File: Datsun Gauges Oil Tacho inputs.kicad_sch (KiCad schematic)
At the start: 11 parts, among them SW1 Oil Pressure Sw, U1 CNY74-4H, U2 CNY74-4H

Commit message: Updated kicad diagrams
Updated kicad diagrams
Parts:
- removed D1, D2: 1N4148, Diode_THT:D_DO-35_SOD27_P7.62mm_Horizontal, symbol Diode:1N4148
- removed R1, R2: 1k8, symbol Device:R
- removed R3, R4: 1k, symbol Device:R
- removed R6: 10R, symbol Device:R
- removed U1, U2: CNY74-4H, symbol Isolator:CNY17-4
- added C3: 100n, symbol Device:C_Small
- added D1, D2: 1N4734A 5.6v, Diode_THT:D_DO-41_SOD81_P10.16mm_Horizontal, symbol Diode:1N47xxA
- added D3: 1N4148, Diode_THT:D_DO-35_SOD27_P7.62mm_Horizontal, symbol Diode:1N4148
- added R1 (x2), R2 (x2): 2k, symbol Device:R
- added U1, U2: 4049, symbol 4xxx:4049
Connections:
- net Arduino Oil Pressure pin: now also U1.2
- net Arduino Tacho pin: now also U2.6
- net Earth: no longer C2.2
- net GND: now also C2.2, D1.2 (A), D2.2 (A), U2.8 (VSS)
- net Oil Pressure Sw input: now also D3.2 (A), R1.2, R2.2
- net Tacho input from ECU: now also R1.2, R2.2
- net VCC: now also U2.1 (VCC)
- net at C2.1: now also D1.1 (K), D3.1 (K), R2.1, U1.3
- new net: D2.1 (K), R2.1, U2.7
- new net VDD: R1.1, R1.1
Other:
- moved on the sheet: SW1

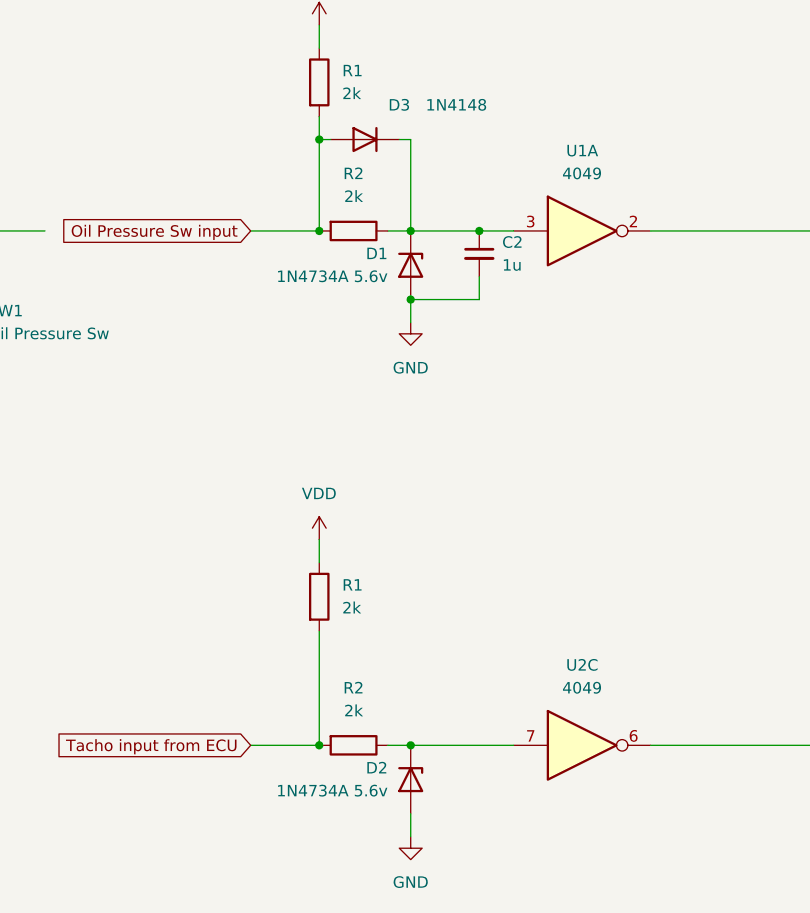
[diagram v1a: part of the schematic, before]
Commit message: Fixes
Changed some switch debouncing
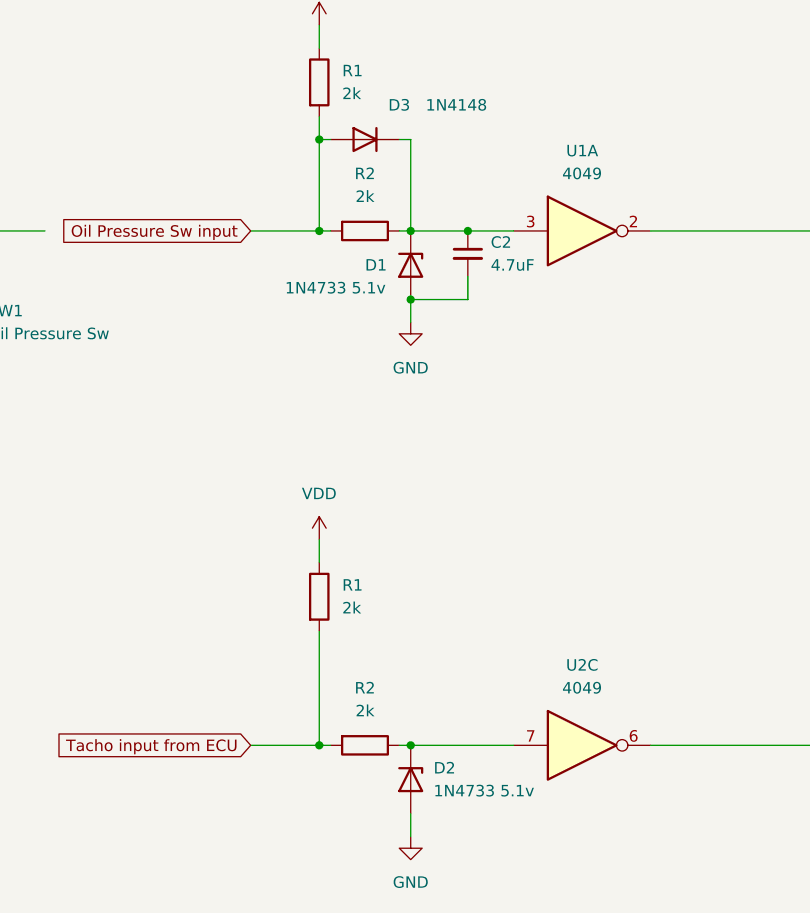
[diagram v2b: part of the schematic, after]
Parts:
- C2: value 1u -> 4.7uF
- D1, D2: value 1N4734A 5.6v -> 1N4733 5.1v
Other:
- moved on the sheet: C2, R2
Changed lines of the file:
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@@
   (junction (at 134.62 77.47) (diameter 0) (color 0 0 0 0)
   )
+  (junction (at 140.97 77.47) (diameter 0) (color 0 0 0 0)
+  )
   (junction (at 124.46 77.47) (diameter 0) (color 0 0 0 0)
   )
@@
   (junction (at 124.46 134.62) (diameter 0) (color 0 0 0 0)
   )
-  (junction (at 142.24 77.47) (diameter 0) (color 0 0 0 0)
-  )
   (junction (at 134.62 85.09) (diameter 0) (color 0 0 0 0)
   )
-  (wire (pts (xy 142.24 82.55) (xy 142.24 85.09))
-    (stroke (width 0) (type default))
-  )
-  (wire (pts (xy 134.62 77.47) (xy 142.24 77.47))
-    (stroke (width 0) (type default))
-  )
-  (wire (pts (xy 132.08 77.47) (xy 134.62 77.47))
+  (wire (pts (xy 140.97 82.55) (xy 140.97 85.09))
+    (stroke (width 0) (type default))
+  )
+  (wire (pts (xy 134.62 77.47) (xy 140.97 77.47))
+    (stroke (width 0) (type default))
+  )
+  (wire (pts (xy 133.35 77.47) (xy 134.62 77.47))
     (stroke (width 0) (type default))
   )
@@
     (stroke (width 0) (type default))
   )
-  (wire (pts (xy 134.62 134.62) (xy 132.08 134.62))
+  (wire (pts (xy 125.73 134.62) (xy 124.46 134.62))
+    (stroke (width 0) (type default))
+  )
+  (wire (pts (xy 134.62 134.62) (xy 133.35 134.62))
     (stroke (width 0) (type default))
   )
@@
     (stroke (width 0) (type default))
   )
-  (wire (pts (xy 142.24 77.47) (xy 146.05 77.47))
+  (wire (pts (xy 140.97 77.47) (xy 146.05 77.47))
     (stroke (width 0) (type default))
   )
@@
     (stroke (width 0) (type default))
   )
-  (wire (pts (xy 134.62 85.09) (xy 142.24 85.09))
+  (wire (pts (xy 134.62 85.09) (xy 140.97 85.09))
     (stroke (width 0) (type default))
   )
@@
   )
   (wire (pts (xy 86.36 77.47) (xy 93.98 77.47))
+    (stroke (width 0) (type default))
+  )
+  (wire (pts (xy 125.73 77.47) (xy 124.46 77.47))
     (stroke (width 0) (type default))
   )
@@
     )
   )
-  (symbol (lib_id "Device:R") (at 128.27 77.47 270) (unit 1)
-    (in_bom yes) (on_board yes) (dnp no) (fields_autoplaced)
-    (property "Reference" "R2" (at 128.27 71.12 90)
-      (effects (font (size 1.27 1.27)))
-    )
-    (property "Value" "2k" (at 128.27 73.66 90)
-      (effects (font (size 1.27 1.27)))
-    )
-    (property "Footprint" "" (at 128.27 75.692 90)
-      (effects (font (size 1.27 1.27)) hide)
-    )
-    (property "Datasheet" "~" (at 128.27 77.47 0)
+  (symbol (lib_id "Device:R") (at 129.54 77.47 270) (unit 1)
+    (in_bom yes) (on_board yes) (dnp no) (fields_autoplaced)
+    (property "Reference" "R2" (at 129.54 71.12 90)
+      (effects (font (size 1.27 1.27)))
+    )
+    (property "Value" "2k" (at 129.54 73.66 90)
+      (effects (font (size 1.27 1.27)))
+    )
+    (property "Footprint" "" (at 129.54 75.692 90)
+      (effects (font (size 1.27 1.27)) hide)
+    )
+    (property "Datasheet" "~" (at 129.54 77.47 0)
       (effects (font (size 1.27 1.27)) hide)
     )
@@
     )
   )
-  (symbol (lib_id "Device:C_Small") (at 142.24 80.01 0) (unit 1)
-    (in_bom yes) (on_board yes) (dnp no) (fields_autoplaced)
-    (property "Reference" "C2" (at 144.78 78.7463 0)
-      (effects (font (size 1.27 1.27)) (justify left))
-    )
-    (property "Value" "1u" (at 144.78 81.2863 0)
-      (effects (font (size 1.27 1.27)) (justify left))
-    )
-    (property "Footprint" "" (at 142.24 80.01 0)
-      (effects (font (size 1.27 1.27)) hide)
-    )
-    (property "Datasheet" "~" (at 142.24 80.01 0)
+  (symbol (lib_id "Device:C_Small") (at 140.97 80.01 0) (unit 1)
+    (in_bom yes) (on_board yes) (dnp no) (fields_autoplaced)
+    (property "Reference" "C2" (at 143.51 78.7463 0)
+      (effects (font (size 1.27 1.27)) (justify left))
+    )
+    (property "Value" "4.7uF" (at 143.51 81.2863 0)
+      (effects (font (size 1.27 1.27)) (justify left))
+    )
+    (property "Footprint" "" (at 140.97 80.01 0)
+      (effects (font (size 1.27 1.27)) hide)
+    )
+    (property "Datasheet" "~" (at 140.97 80.01 0)
       (effects (font (size 1.27 1.27)) hide)
     )
@@
   (symbol (lib_id "Diode:1N47xxA") (at 134.62 138.43 270) (unit 1)
     (in_bom yes) (on_board yes) (dnp no) (fields_autoplaced)
-    (property "Reference" "D2" (at 132.08 137.16 90)
-      (effects (font (size 1.27 1.27)) (justify right))
-    )
-    (property "Value" "1N4734A 5.6v" (at 132.08 139.7 90)
-      (effects (font (size 1.27 1.27)) (justify right))
+    (property "Reference" "D2" (at 137.16 137.16 90)
+      (effects (font (size 1.27 1.27)) (justify left))
+    )
+    (property "Value" "1N4733 5.1v" (at 137.16 139.7 90)
+      (effects (font (size 1.27 1.27)) (justify left))
     )
     (property "Footprint" "Diode_THT:D_DO-41_SOD81_P10.16mm_Horizontal" (at 130.175 138.43 0)
@@
   )
   (symbol (lib_id "Diode:1N47xxA") (at 134.62 81.28 270) (unit 1)
-    (in_bom yes) (on_board yes) (dnp no) (fields_autoplaced)
-    (property "Reference" "D1" (at 132.08 80.01 90)
-      (effects (font (size 1.27 1.27)) (justify right))
-    )
-    (property "Value" "1N4734A 5.6v" (at 132.08 82.55 90)
-      (effects (font (size 1.27 1.27)) (justify right))
+    (in_bom yes) (on_board yes) (dnp no)
+    (property "Reference" "D1" (at 129.54 81.28 90)
+      (effects (font (size 1.27 1.27)) (justify left))
+    )
+    (property "Value" "1N4733 5.1v" (at 120.65 83.82 90)
+      (effects (font (size 1.27 1.27)) (justify left))
     )
     (property "Footprint" "Diode_THT:D_DO-41_SOD81_P10.16mm_Horizontal" (at 130.175 81.28 0)
@@
     )
   )
-  (symbol (lib_id "Device:R") (at 128.27 134.62 270) (unit 1)
-    (in_bom yes) (on_board yes) (dnp no) (fields_autoplaced)
-    (property "Reference" "R2" (at 128.27 128.27 90)
-      (effects (font (size 1.27 1.27)))
-    )
-    (property "Value" "2k" (at 128.27 130.81 90)
-      (effects (font (size 1.27 1.27)))
-    )
-    (property "Footprint" "" (at 128.27 132.842 90)
-      (effects (font (size 1.27 1.27)) hide)
-    )
-    (property "Datasheet" "~" (at 128.27 134.62 0)
-      (effects (font (size 1.27 1.27)) hide)
-    )
+  (symbol (lib_id "Device:R") (at 129.54 134.62 270) (unit 1)
+    (in_bom yes) (on_board yes) (dnp no) (fields_autoplaced)
+    (property "Reference" "R2" (at 129.54 128.27 90)
+      (effects (font (size 1.27 1.27)))
+    )
+    (property "Value" "2k" (at 129.54 130.81 90)
+      (effects (font (size 1.27 1.27)))
+    )
+    (property "Footprint" "" (at 129.54 132.842 90)
+      (effects (font (size 1.27 1.27)) hide)
+    )
+    (property "Datasheet" "~" (at 129.54 134.62 0)
+      (effects (font (size 1.27 1.27)) hide)
+    )

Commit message: Cleanup
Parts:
- removed C2: 4.7uF, symbol Device:C_Small
- removed D1: 1N4733 5.1v, Diode_THT:D_DO-41_SOD81_P10.16mm_Horizontal, symbol Diode:1N47xxA
- added C3: 4.7uF, symbol Device:C_Polarized_Small
- R1, R2: value 2k -> 8k2
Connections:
- net GND: now also C3.2
- net VCC: now also R1.1
- net VDD: no longer R1.1
- net at D3.1 (K), R2.1, U1.3: now also C3.1
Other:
- moved on the sheet: D2
